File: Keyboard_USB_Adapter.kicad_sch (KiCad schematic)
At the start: 9 parts, among them J1 USB_C_Receptacle_USB2.0_16P, J2 Conn_01x05, SW1 SW_SPDT, U1 USBLC6-2SC6

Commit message: Progress
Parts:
- C1: value C -> 10nF
- C2: value C -> 100nF
- F1: value Polyfuse -> 500mA
- R1, R2: value R -> 5.1K
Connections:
- net GND: now reaches J1.A1 (GND), J1.A12 (GND), J1.B1 (GND), J1.B12 (GND)
- net GND: now also J1.SH (SHIELD), R1.1, R2.1
- net VBUS: now reaches J1.A4 (VBUS), J1.A9 (VBUS), J1.B4 (VBUS), J1.B9 (VBUS)
- net at J1.A5 (CC1): now also R2.2
- net at J1.A6 (D+): now also J1.B6 (D+)
- net at J1.A7 (D-): now also J1.B7 (D-)
- net at J1.B5 (CC2): now also R1.2
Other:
- moved on the sheet: F1, J1, J2, R1, R2, SW1

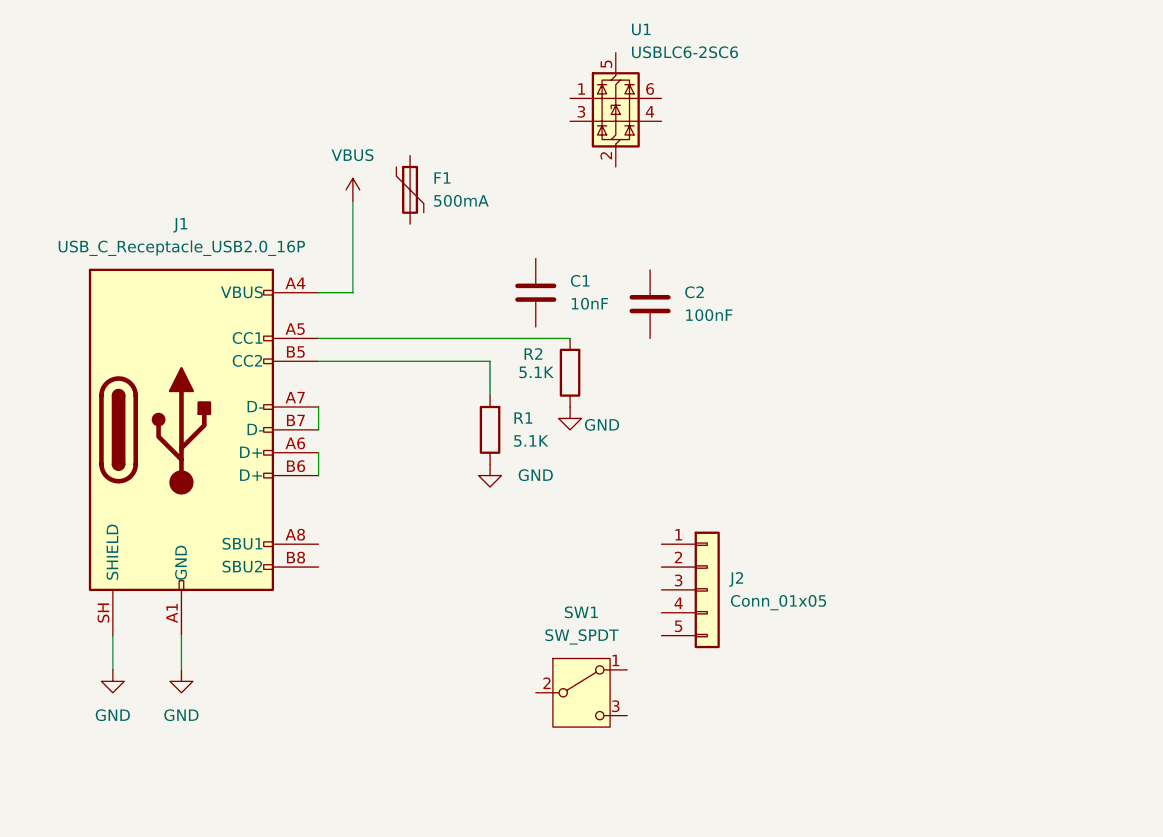
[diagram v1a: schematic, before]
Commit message: updated a lot of labels
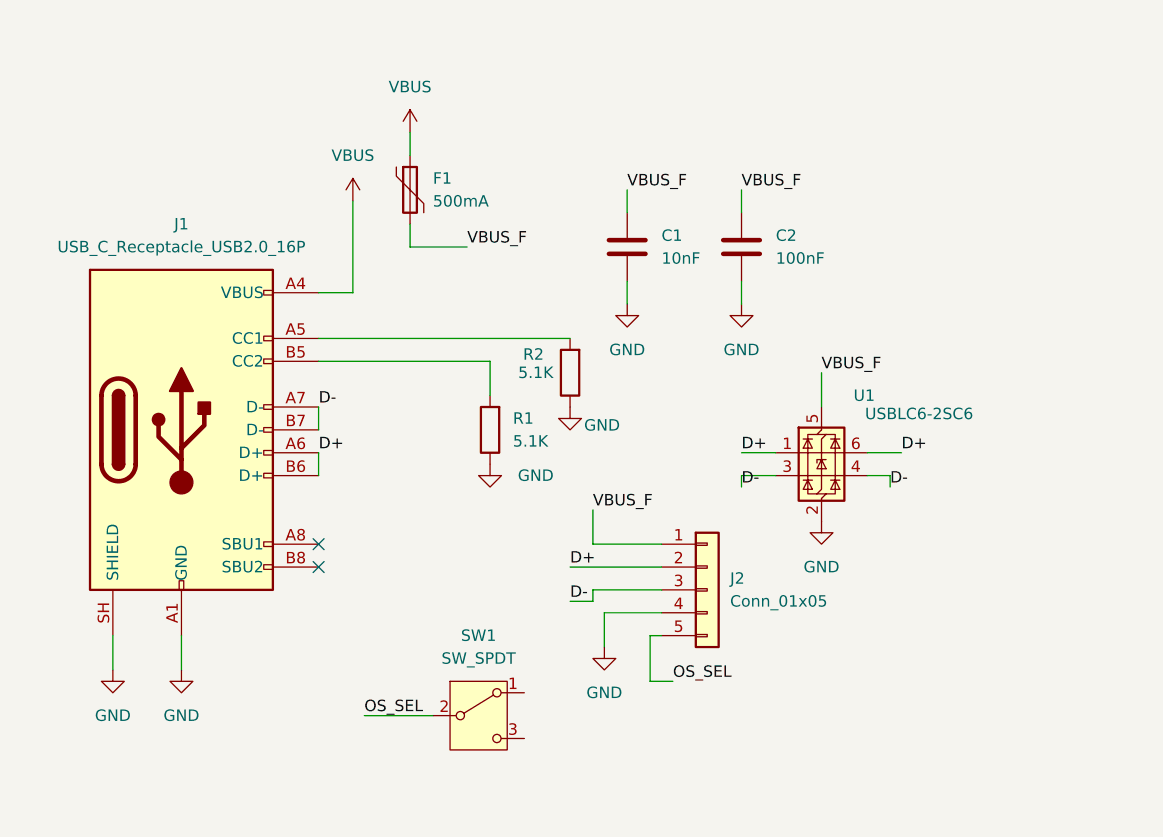
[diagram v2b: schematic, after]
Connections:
- net GND: now also C1.2, C2.2, J2.4 (Pin_4), U1.2 (GND)
- net VBUS: now also F1.1
- net at J1.A6 (D+), J1.B6 (D+): no longer names the net of J1.A6 (D+), J1.B6 (D+)
- net at J1.A6 (D+), J1.B6 (D+): now also J2.2 (Pin_2), U1.1 (I/O1), U1.6 (I/O1)
- net D-: now reaches J1.A7 (D-), J1.B7 (D-)
- net D-: now also J2.3 (Pin_3), U1.3 (I/O2), U1.4 (I/O2)
- net VBUS_F: now reaches C2.1
- net VBUS_F: now also C1.1, F1.2, J2.1 (Pin_1), U1.5 (VBUS)
- net OS_SEL: now reaches SW1.2 (B)
- net OS_SEL: now also J2.5 (Pin_5)
- no-connect marks 0 -> 2
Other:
- moved on the sheet: C1, C2, SW1, U1

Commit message: Schematic should be done now
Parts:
- C1: value 10nF -> 10uF
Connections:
- net D-: now also J2.2 (Pin_2); no longer J2.3 (Pin_3)
- net GND: now also SW1.3 (C)
- net at J1.A6 (D+), J1.B6 (D+), U1.1 (I/O1)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: now also J2.3 (Pin_3); no longer J2.2 (Pin_2)
- no-connect marks 2 -> 3
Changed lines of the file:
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@@
+	)
+	(no_connect
+		(at 80.01 120.65)
 	)
 	(no_connect
@@
 		(pts
 			(xy 85.09 110.49) (xy 87.63 110.49)
+		)
+		(stroke
+			(width 0)
+			(type default)
+		)
+	)
+	(wire
+		(pts
+			(xy 80.01 125.73) (xy 82.55 125.73)
+		)
+		(stroke
+			(width 0)
+			(type default)
+		)
+	)
+	(wire
+		(pts
+			(xy 82.55 125.73) (xy 82.55 128.27)
 		)
 		(stroke
@@
 		)
 	)
-	(label "D-"
+	(label "D+"
 		(at 85.09 110.49 0)
 		(effects
@@
 		)
 	)
-	(label "D+"
+	(label "D-"
 		(at 85.09 106.68 0)
 		(effects
@@
 	)
 	(symbol
+		(lib_id "power:GND")
+		(at 82.55 128.27 0)
+		(unit 1)
+		(body_style 1)
+		(exclude_from_sim no)
+		(in_bom yes)
+		(on_board yes)
+		(in_pos_files yes)
+		(dnp no)
+		(fields_autoplaced yes)
+		(property "Reference" "#PWR011"
+			(at 82.55 134.62 0)
+			(hide yes)
+			(show_name no)
+			(do_not_autoplace no)
+			(effects
+				(font
+					(size 1.27 1.27)
+				)
+			)
+		)
+		(property "Value" "GND"
+			(at 82.55 133.35 0)
+			(show_name no)
+			(do_not_autoplace no)
+			(effects
+				(font
+					(size 1.27 1.27)
+				)
+			)
+		)
+		(property "Footprint" ""
+			(at 82.55 128.27 0)
+			(hide yes)
+			(show_name no)
+			(do_not_autoplace no)
+			(effects
+				(font
+					(size 1.27 1.27)
+				)
+			)
+		)
+		(property "Datasheet" ""
+			(at 82.55 128.27 0)
+			(hide yes)
+			(show_name no)
+			(do_not_autoplace no)
+			(effects
+				(font
+					(size 1.27 1.27)
+				)
+			)
+		)
+		(property "Description" "Power symbol creates a global label with name \"GND\" , ground"
+			(at 82.55 128.27 0)
+			(hide yes)
+			(show_name no)
+			(do_not_autoplace no)
+			(effects
+				(font
+					(size 1.27 1.27)
+				)
+			)
+		)
+		(pin "1"
+		)
+		(instances
+			(project "Keyboard_USB_Adapter"
+				(path "/5abeb7b7-6d19-4686-bb3f-ba353c7d837b"
+					(reference "#PWR011")
+					(unit 1)
+				)
+			)
+		)
+	)
+	(symbol
 		(lib_id "Device:R")
 		(at 76.2 91.44 180)
@@
 			)
 		)
-		(property "Value" "10nF"
+		(property "Value" "10uF"
 			(at 95.25 72.3899 0)
 			(show_name no)
